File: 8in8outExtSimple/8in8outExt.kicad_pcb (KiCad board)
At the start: 2 copper layers, 101.6 x 42 mm, 72 parts, among them P1 CONN_10X2, Q1 PNP, Q10 NPN, Q11 NPN, Q12 NPN, Q13 NPN, Q14 NPN, Q15 NPN, Q16 NPN, Q2 PNP, Q3 PNP, Q4 PNP, Q5 PNP, Q6 PNP, Q7 PNP, Q8 PNP, Q9 NPN

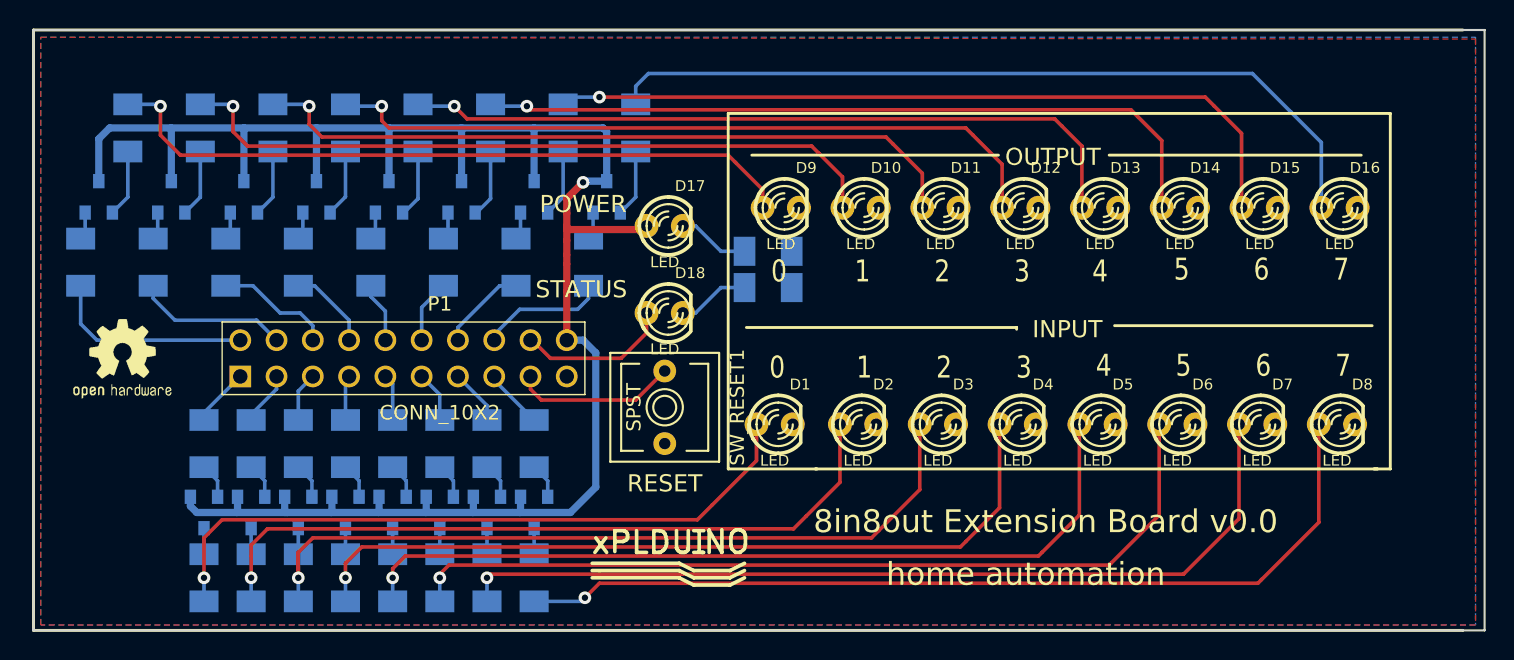
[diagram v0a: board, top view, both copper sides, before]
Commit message: agrandissement taille du panneau ajout NPN pour commande led status serigraphie
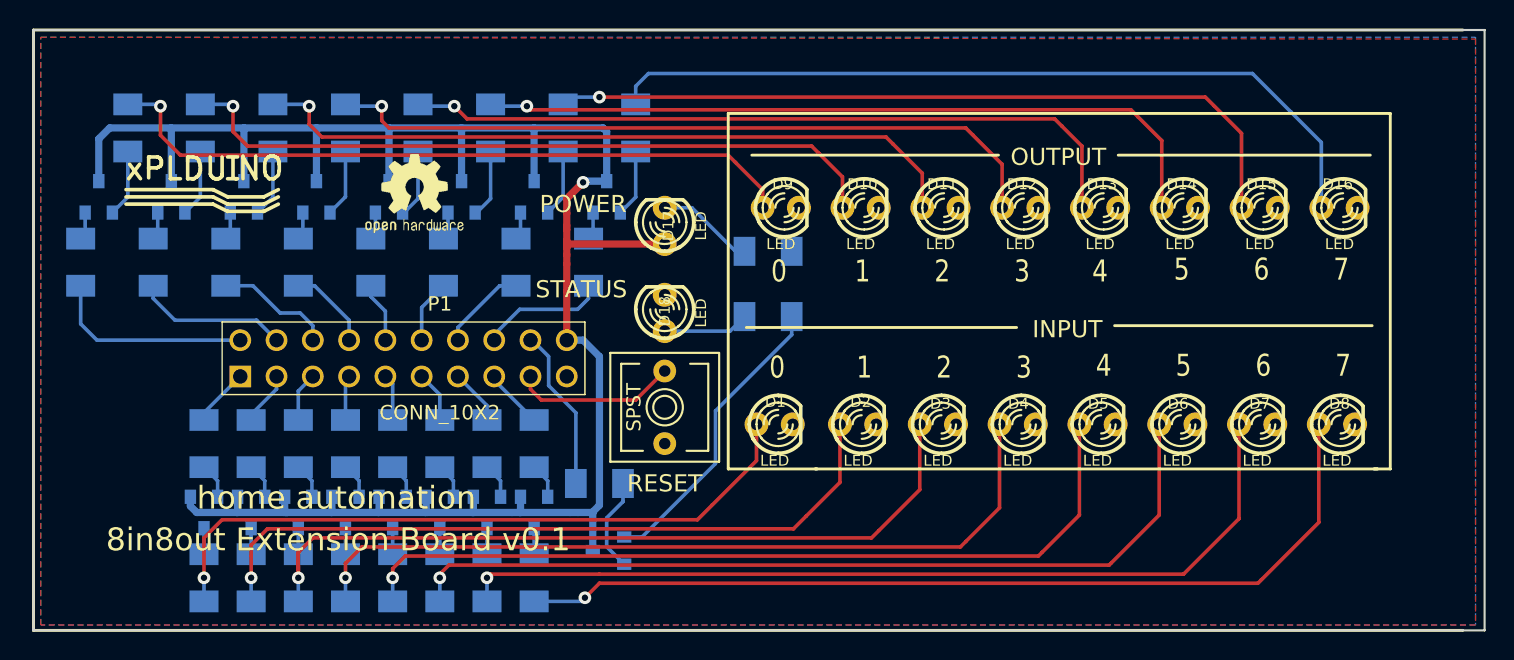
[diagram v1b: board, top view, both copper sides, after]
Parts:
- added Q19: NPN, SOT23, B.Cu at (126.6, 110.4)
- added R43: R, SM1206, B.Cu at (126.0, 105.7)
- moved logo_xplduino 41.8 mm to (98.2, 85.3)
- moved G*** 23.5 mm to (109.2, 81.7)
- moved R42 2.03 mm to (137.8, 94.0), turned to 0 degrees
- turned D17 to 90 degrees
- turned D18 to 90 degrees
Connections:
- D18 pad 1: LED -> N-0000054
- D18 pad 2: N-0000067 (its old number) -> GND
- R42 pad 1: GND -> N-0000054
- R42 pad 2: N-0000067 (its old number) -> N-0000036
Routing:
- net N-0000036: track 0.00 -> 21.0 mm
- net N-0000037: track 0.00 -> 6.63 mm
- net N-0000054: track 0.00 -> 6.01 mm
- net +5V: track 133.7 -> 138.9 mm
- net N-0000067 (its old number): track 5.05 -> 0.00 mm
- net N-0000055: track 5.05 -> 6.85 mm
- net LED: track 10.8 -> 11.4 mm
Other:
- board text added: "8in8out Extension Board v0.1"
- board text removed: "8in8out Extension Board v0.0"

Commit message: ?change package SOT23 des transistors: 1.B 2.E 3.C au lieu de 1.E 2.B 3.C
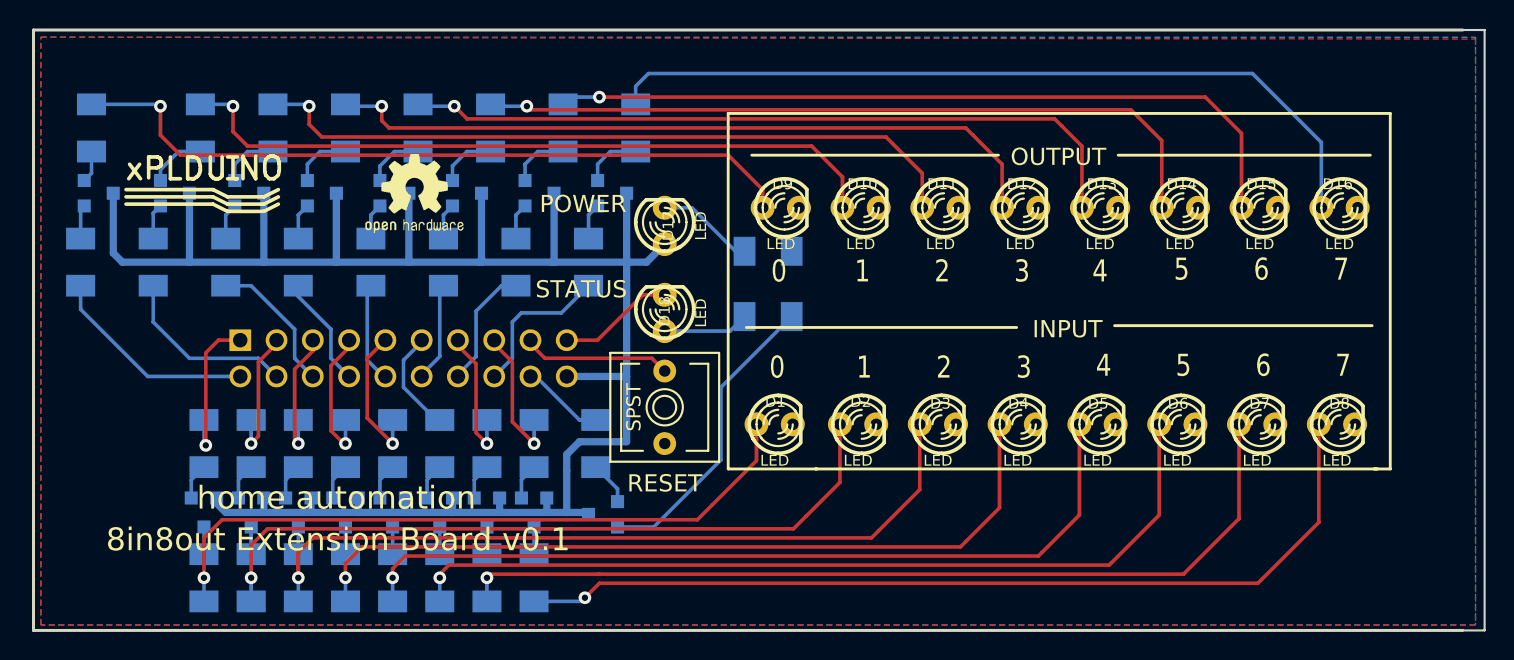
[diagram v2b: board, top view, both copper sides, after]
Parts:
- P1: moved to B.Cu
- Q1, Q10, Q11, Q12, Q13, Q14, Q15, Q16, Q19, Q2, Q3, Q4, Q5, Q6, Q7, Q8, Q9: footprint SOT23 -> SOT23EBC
- moved R43 2.81 mm to (125.7, 102.9), turned to 270 degrees
- moved Q19 2.57 mm to (126.2, 107.8), turned to 90 degrees
- moved R33 2.54 mm to (90.4, 80.8)
- moved Q11 0.46 mm to (101.5, 85.3), turned to 270 degrees
- moved Q12 0.46 mm to (106.6, 85.3), turned to 270 degrees
- moved Q13 0.46 mm to (111.6, 85.3), turned to 270 degrees
- moved Q14 0.46 mm to (116.7, 85.3), turned to 270 degrees
- moved Q15 0.46 mm to (121.8, 85.3), turned to 270 degrees
- moved Q16 0.46 mm to (126.9, 85.3), turned to 270 degrees
- moved Q10 0.36 mm to (96.3, 85.3), turned to 270 degrees
- moved Q9 0.25 mm to (90.9, 85.3), turned to 270 degrees
- turned Q1 to 180 degrees
- turned Q2 to 180 degrees
- turned Q3 to 180 degrees
- turned Q4 to 180 degrees
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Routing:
- net GND: track 0.00 -> 8.17 mm
- net CMD0: track 4.10 -> 11.1 mm, vias 0 -> 1
- net CMD4: track 3.26 -> 10.2 mm, vias 0 -> 1
- net CMD3: track 3.15 -> 9.91 mm, vias 0 -> 1
- net CMD2: track 3.47 -> 9.52 mm, vias 0 -> 1
- net CMD7: track 4.21 -> 10.0 mm, vias 0 -> 1
- net CMD6: track 3.89 -> 9.73 mm, vias 0 -> 1
- net CMD1: track 3.78 -> 9.63 mm, vias 0 -> 1
- net LED: track 11.4 -> 5.83 mm
- net CMD5: track 3.57 -> 7.31 mm
- net N-0000037: track 6.63 -> 3.04 mm
- net OUT4: track 4.23 -> 7.06 mm
- net OUT5: track 4.44 -> 6.98 mm
- net N-000009: track 49.4 -> 51.9 mm
- net N-000007: track 4.72 -> 2.24 mm
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
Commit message: correction erreur schema led out5 pas reli? au GND
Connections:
- D14 pad 2: N-0000034 (its old number) -> GND
